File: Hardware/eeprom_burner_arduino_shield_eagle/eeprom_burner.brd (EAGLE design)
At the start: 45.2 x 50 mm, 7 parts, among them IC2 74LS595N, IC3 74LS595N

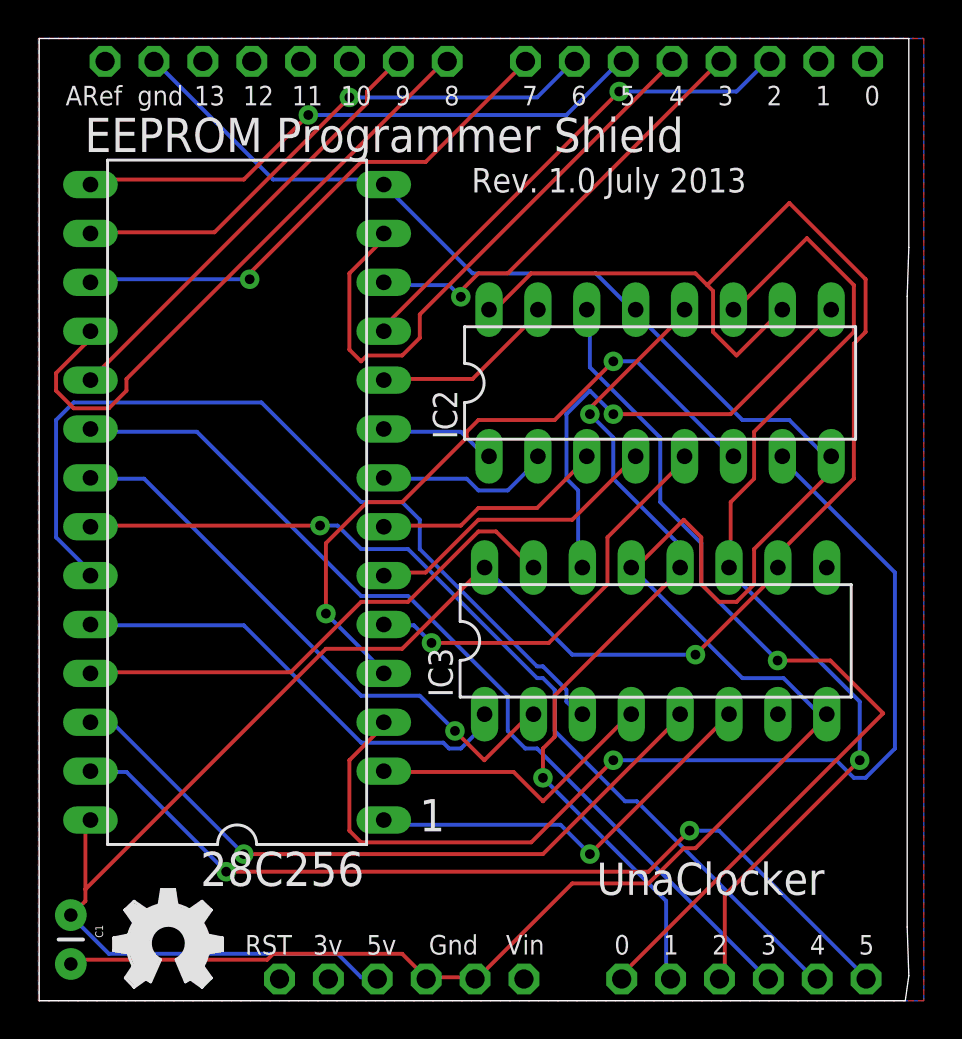
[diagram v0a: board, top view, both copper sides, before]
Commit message: Python CLI, Paged Write, Unlocker
Fleshed out python command line interface
Added paged write and unlock functions
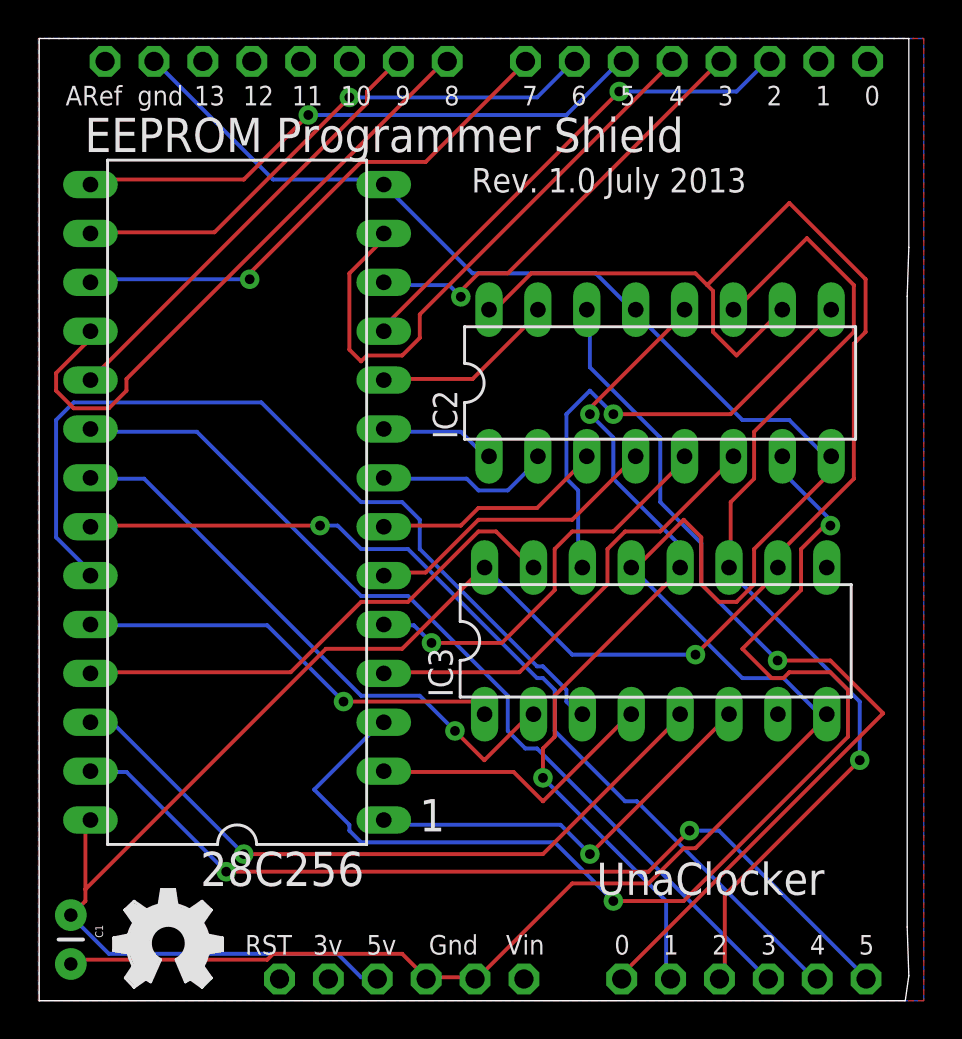
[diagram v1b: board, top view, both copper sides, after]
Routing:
- net N$18: track 35.4 -> 24.0 mm, vias 2 -> 0
- net N$19: track 55.4 -> 61.0 mm, vias 1 -> 2
- net N$22: track 24.5 -> 22.4 mm, vias 0 -> 1
